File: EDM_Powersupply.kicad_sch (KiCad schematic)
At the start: 6 parts, among them Q1 IRF60DM206

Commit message: Simulation 7-may
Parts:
- removed Q1: IRF60DM206, Package_DirectFET:DirectFET_ME, symbol Transistor_FET:IRF60DM206
- removed R3: 10k, symbol Device:R
- removed V1: VPULSE, symbol Simulation_SPICE:VPULSE
- removed V2: 100, symbol Simulation_SPICE:VDC
- added Q1: IRF3205, Package_TO_SOT_THT:TO-220-3_Vertical, symbol Transistor_FET:IRF3205
- added R5: 100, symbol Device:R
- added R6: 10k, symbol Device:R
- added U1: MCP1416R, Package_TO_SOT_SMD:SOT-23-5, symbol Driver_FET:MCP1416R
- added V3, V5: 10, symbol Simulation_SPICE:VDC
- added V4: VPULSE, symbol Simulation_SPICE:VPULSE
- R1: value 100 -> 10k
- R2: value 100 -> 10
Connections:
- net 0: now also Q1.3 (S), R6.1, U1.2 (GND), V3.2, V4.2, V5.2
- net at R2.2: now also Q1.2 (D)
- net at R1.1: now also Q1.1 (G)
- net at R2.1: now also V5.1
- net at R1.2: now also U1.4 (OUT)
- new net: R5.1, V4.1
- new net: R5.2, R6.2, U1.3 (IN)
- new net: U1.5 (Vdd), V3.1

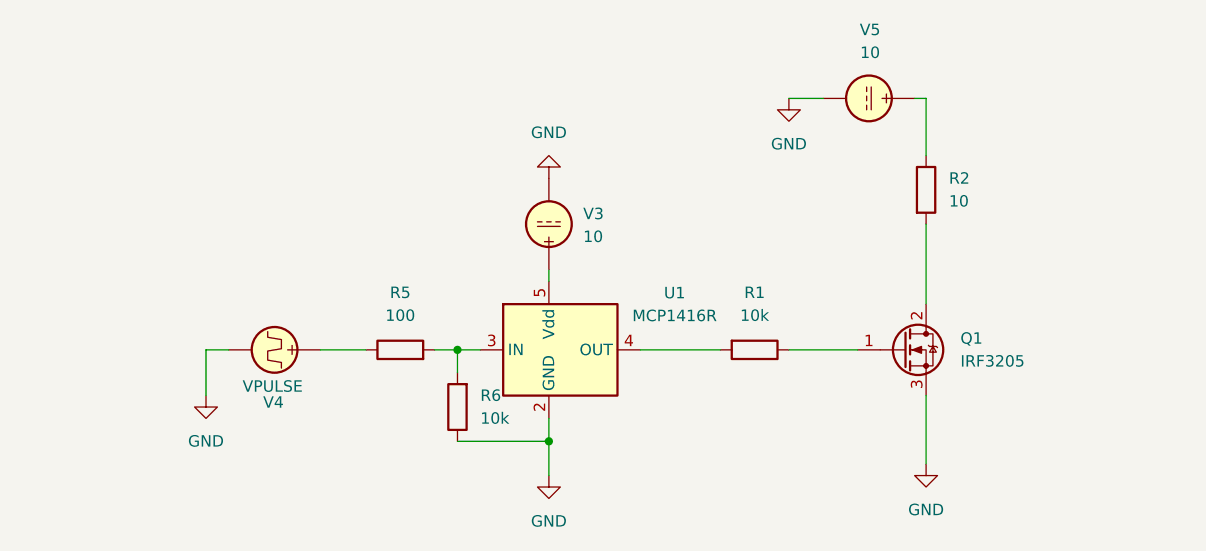
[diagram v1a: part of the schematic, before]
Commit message: Simulation fixed + some default NMOS testing files
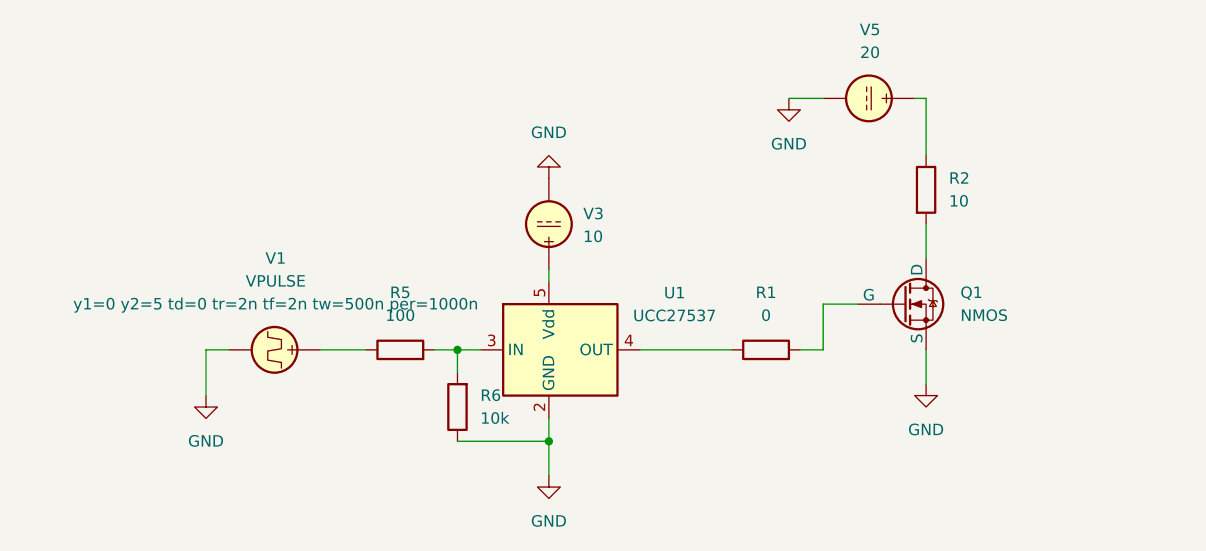
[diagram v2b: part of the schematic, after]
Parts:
- removed Q1: IRF3205, Package_TO_SOT_THT:TO-220-3_Vertical, symbol Transistor_FET:IRF3205
- removed V4: VPULSE, symbol Simulation_SPICE:VPULSE
- added Q1: NMOS, symbol Simulation_SPICE:NMOS
- added V1: VPULSE, symbol Simulation_SPICE:VPULSE
- R1: value 10k -> 0
- U1: value MCP1416R -> UCC27537
- V5: value 10 -> 20
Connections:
- net 0: now also Q1.3 (S), V1.2
- net at R5.1: now also V1.1
- net at U1.4 (OUT): now also R1.1; no longer R1.2
- net at R2.2: now also Q1.1 (D)
- new net: Q1.2 (G), R1.2

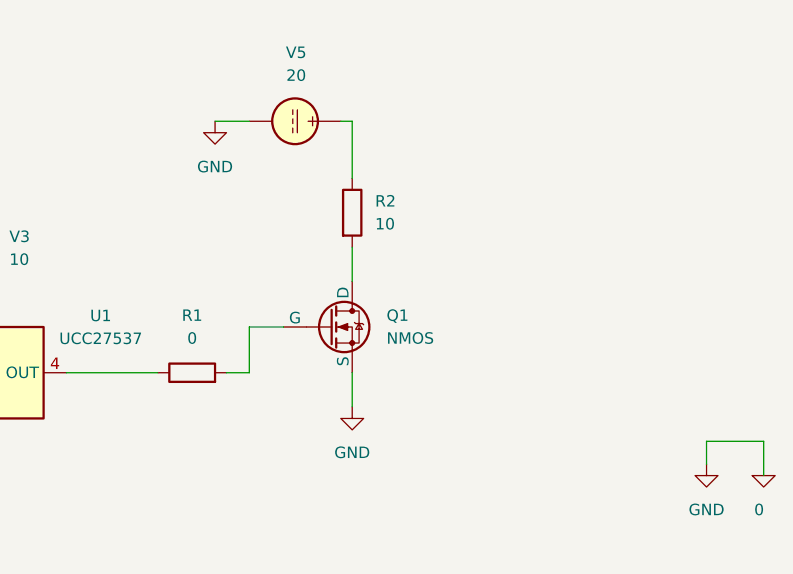
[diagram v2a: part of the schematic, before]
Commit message: Fixed small mistake in simulation + added the IPW NMOS properly
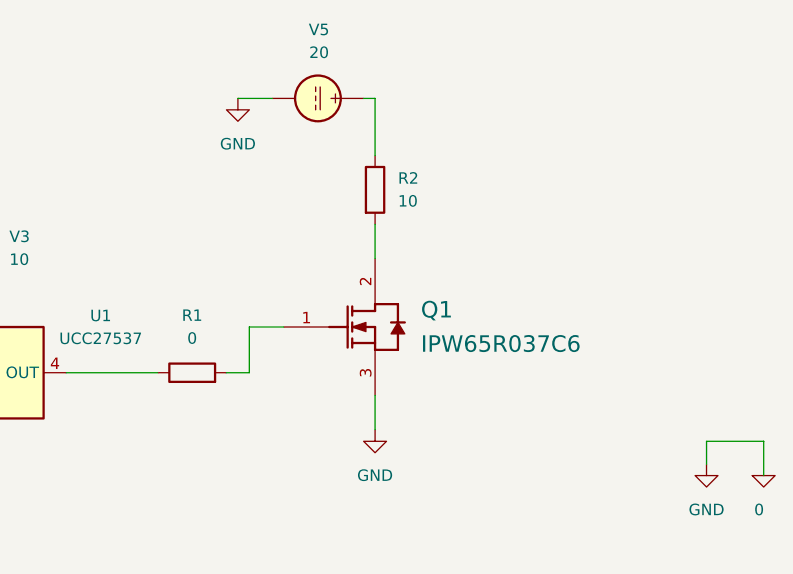
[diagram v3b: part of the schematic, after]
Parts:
- removed Q1: NMOS, symbol Simulation_SPICE:NMOS
- added Q1: IPW65R037C6, INF-PG-TO247-3-44, symbol IPW65R037C6:IPW65R037C6
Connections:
- net 0: now also Q1.3 (SOURCE)
- net at R2.2: now also Q1.2 (DRAIN)
- net at R1.2: now also Q1.1 (GATE)
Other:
- moved on the sheet: R2, V5

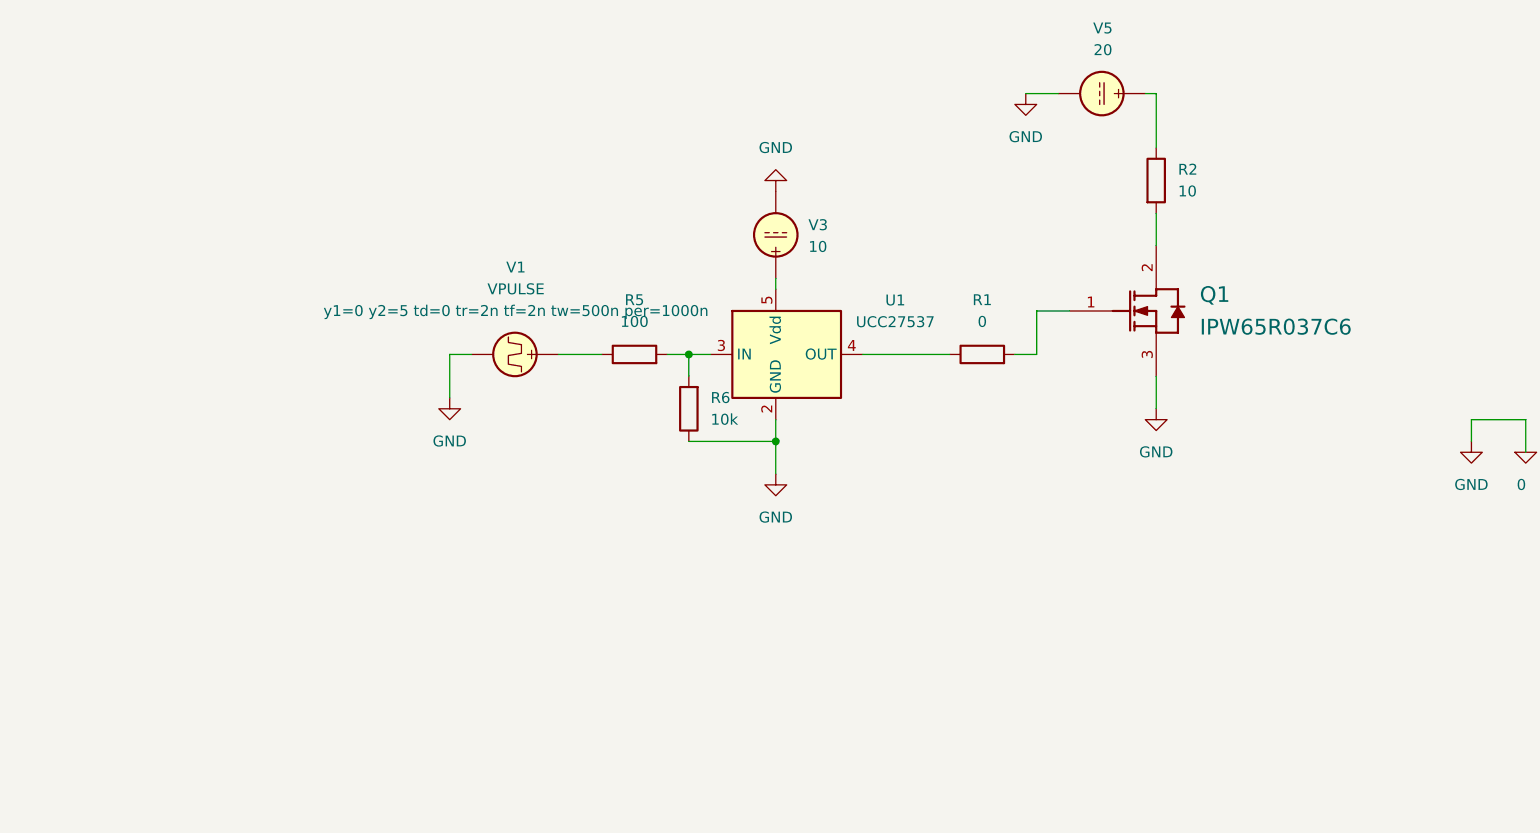
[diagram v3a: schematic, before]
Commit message: Added the UCC gate driver sim model + footprint
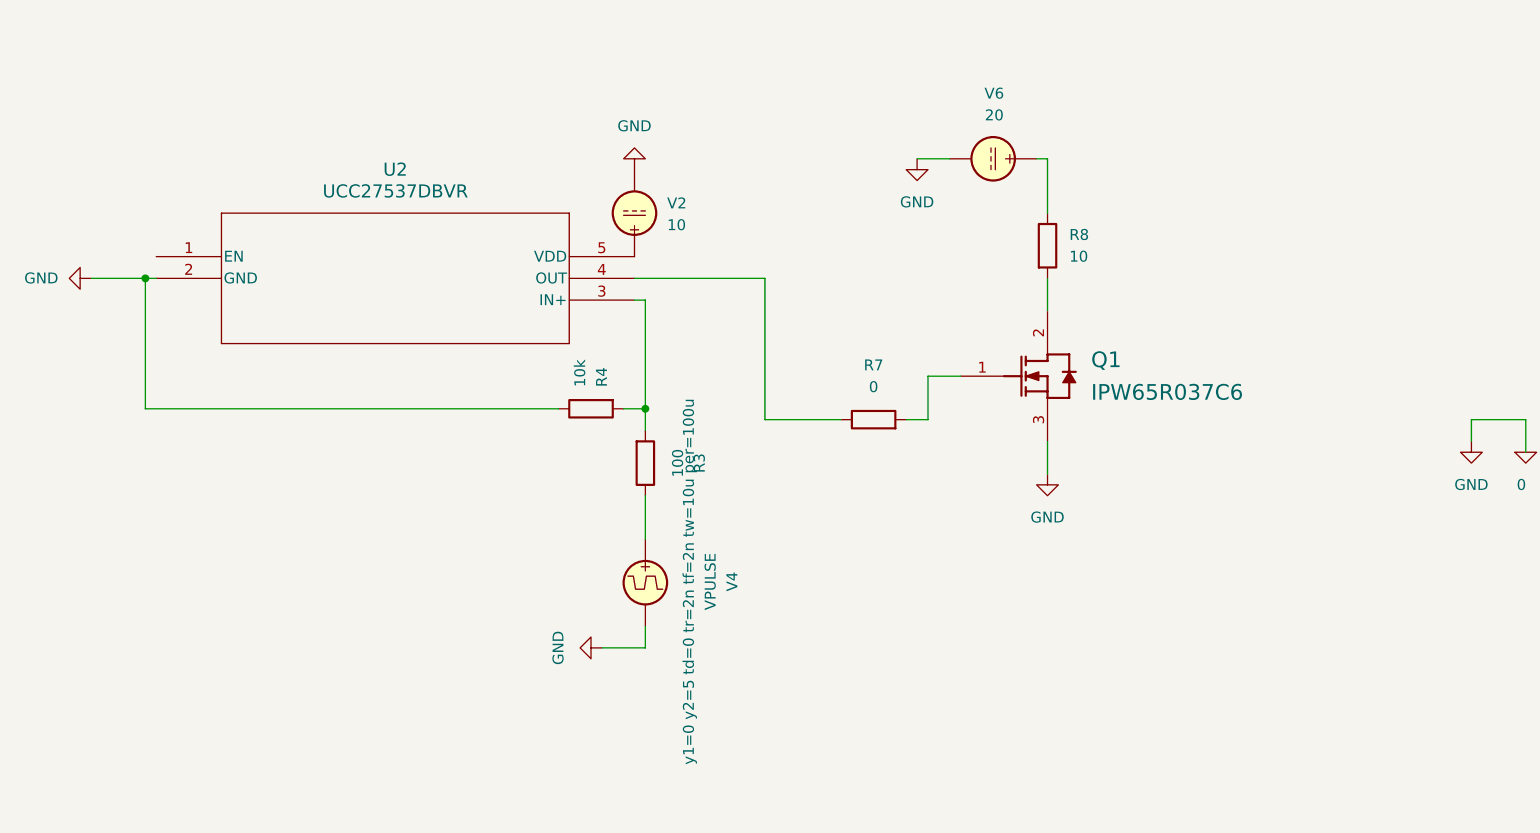
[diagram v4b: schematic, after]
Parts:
- removed R1: 0, symbol Device:R
- removed R2: 10, symbol Device:R
- removed R5: 100, symbol Device:R
- removed R6: 10k, symbol Device:R
- removed U1: UCC27537, Package_TO_SOT_SMD:SOT-23-5, symbol Driver_FET:MCP1416R
- removed V1: VPULSE, symbol Simulation_SPICE:VPULSE
- removed V3: 10, symbol Simulation_SPICE:VDC
- removed V5: 20, symbol Simulation_SPICE:VDC
- added R3: 100, symbol Device:R
- added R4: 10k, symbol Device:R
- added R7: 0, symbol Device:R
- added R8: 10, symbol Device:R
- added U2: UCC27537DBVR, DBV5_TEX, symbol 2024-05-09_09-23-31:UCC27537DBVR
- added V2: 10, symbol Simulation_SPICE:VDC
- added V4: VPULSE, symbol Simulation_SPICE:VPULSE
- added V6: 20, symbol Simulation_SPICE:VDC
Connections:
- net 0: now also R4.1, U2.2 (GND), V2.2, V4.2, V6.2
- net at Q1.2 (DRAIN): now also R8.2
- net at Q1.1 (GATE): now also R7.2
- new net: R7.1, U2.4 (OUT)
- new net: U2.5 (VDD), V2.1
- new net: R3.1, V4.1
- new net: R8.1, V6.1
- new net: R3.2, R4.2, U2.3 (IN+)

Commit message: improved layout
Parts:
- removed R7: 0, symbol Device:R
- removed R8: 10, symbol Device:R
- removed U2: UCC27537DBVR, DBV5_TEX, symbol 2024-05-09_09-23-31:UCC27537DBVR
- removed V4: VPULSE, symbol Simulation_SPICE:VPULSE
- removed V6: 20, symbol Simulation_SPICE:VDC
- added C1, C5: 0.33u, symbol Device:C
- added C2, C6: 0.1u, symbol Device:C
- added C3: 100n, symbol Device:C
- added C4: 1u, symbol Device:C
- added R1, R2: 10, symbol Device:R
- added R5: 10k, symbol Device:R
- added U1: L7805, Package_TO_SOT_THT:TO-220-3_Vertical, symbol Regulator_Linear:L7805
- added U2: STGAP2SM, Package_SO:SOIC-8_3.9x4.9mm_P1.27mm, symbol Driver_FET:STGAP2SM
- added U3: RP2040, Package_DFN_QFN:QFN-56-1EP_7x7mm_P0.4mm_EP3.2x3.2mm, symbol MCU_RaspberryPi:RP2040
- added U4: L7815, symbol Regulator_Linear:L7815
- added V1: 24, symbol Simulation_SPICE:VDC
- added V3: VPULSE, symbol Simulation_SPICE:VPULSE
- R3: value 100 -> 10
- R4: value 10k -> 10
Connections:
- net at Q1.1 (GATE): now also R1.2, R2.2
- net +VDC: now reaches V2.1
- net +VDC: now also R3.1
- net at R3.2: now also Q1.2 (DRAIN); no longer R4.2
- net 0 renamed GND
- net GND: now also C1.2, C2.2, C3.2, C4.2, C5.2, C6.2, R5.1, U1.2 (GND), U2.3 (IN-), U2.4 (GND), U2.8 (GNDISO), U4.2 (GND), V1.2, V3.2; no longer R4.1
- new net: R2.1, U2.6 (GON)
- new net: R1.1, U2.7 (GOFF)
- new net: R4.2, R5.2, U2.2 (IN+)
- new net: U3.1 (IOVDD), U3.10 (IOVDD), U3.22 (IOVDD), U3.33 (IOVDD), U3.42 (IOVDD), U3.49 (IOVDD)
- new net: U3.23 (DVDD), U3.50 (DVDD)
- new net +15V: C6.1, U2.5 (VH), U4.3 (OUT)
- new net +24V: C1.1, C5.1, U1.1 (IN), U4.1 (IN), V1.1
- new net +5V: C2.1, C3.1, C4.1, U1.3 (OUT), U2.1 (VDD)
- new net PWM: R4.1, V3.1
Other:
- note added: ".options abstol=1e-10"
- note added: ".options cshunt=1e-15"
- note added: ".options gmin=1e-10"
- note added: ".options reltol=0.003"
- note added: "15V regulation"
- note added: "5V regulation"
- note added: "ISOLATION"
- note added: "Main Transistor Driver"
- note added: "Microcontroller"
- note added: "Spice Simulation"
- note added: "optional"
- moved on the sheet: Q1
